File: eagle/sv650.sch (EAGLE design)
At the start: 22 parts, among them IC1 7805

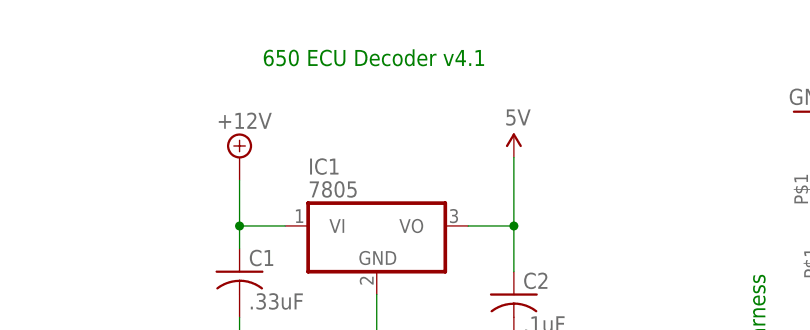
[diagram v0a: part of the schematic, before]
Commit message: update to show v4.2 and date
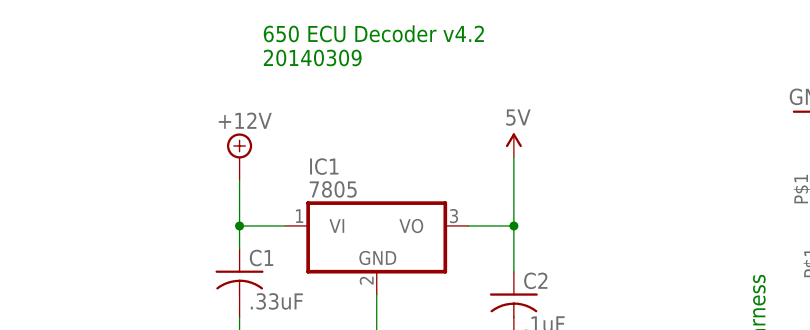
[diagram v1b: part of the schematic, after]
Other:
- note added: "650 ECU Decoder v4.2 20140309"
- note removed: "650 ECU Decoder v4.1"
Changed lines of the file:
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@@
 <plain>
 <text x="114.3" y="68.58" size="1.778" layer="91" rot="R90">To Wiring Harness</text>
-<text x="58.42" y="111.76" size="1.778" layer="91">650 ECU Decoder v4.1</text>
+<text x="58.42" y="111.76" size="1.778" layer="91">650 ECU Decoder v4.2
+20140309</text>
 </plain>
 <instances>
@@
 </schematic>
 </drawing>
+<compatibility>
+<note version="6.3" minversion="6.2.2" severity="warning">
+Since Version 6.2.2 text objects can contain more than one line,
+which will not be processed correctly with this version.
+</note>
+</compatibility>
 </eagle>

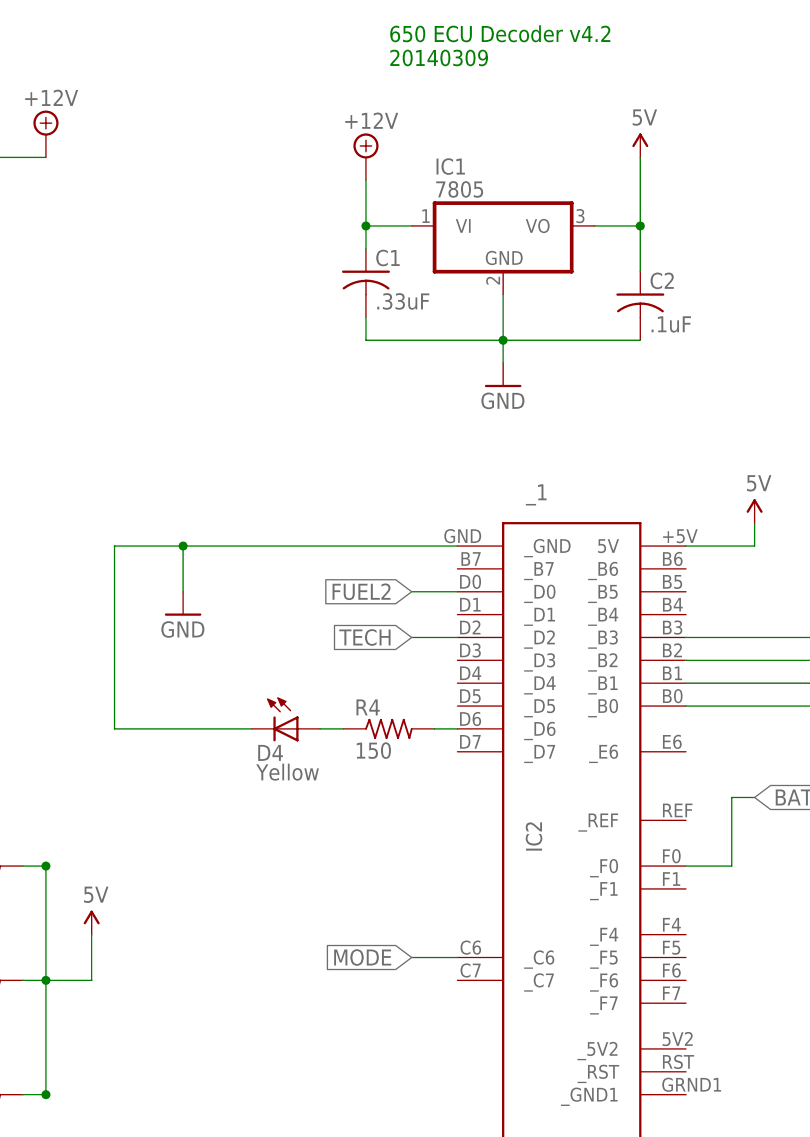
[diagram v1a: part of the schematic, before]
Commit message: change mode button to pin D1/6 so we can assign an interrupt to it
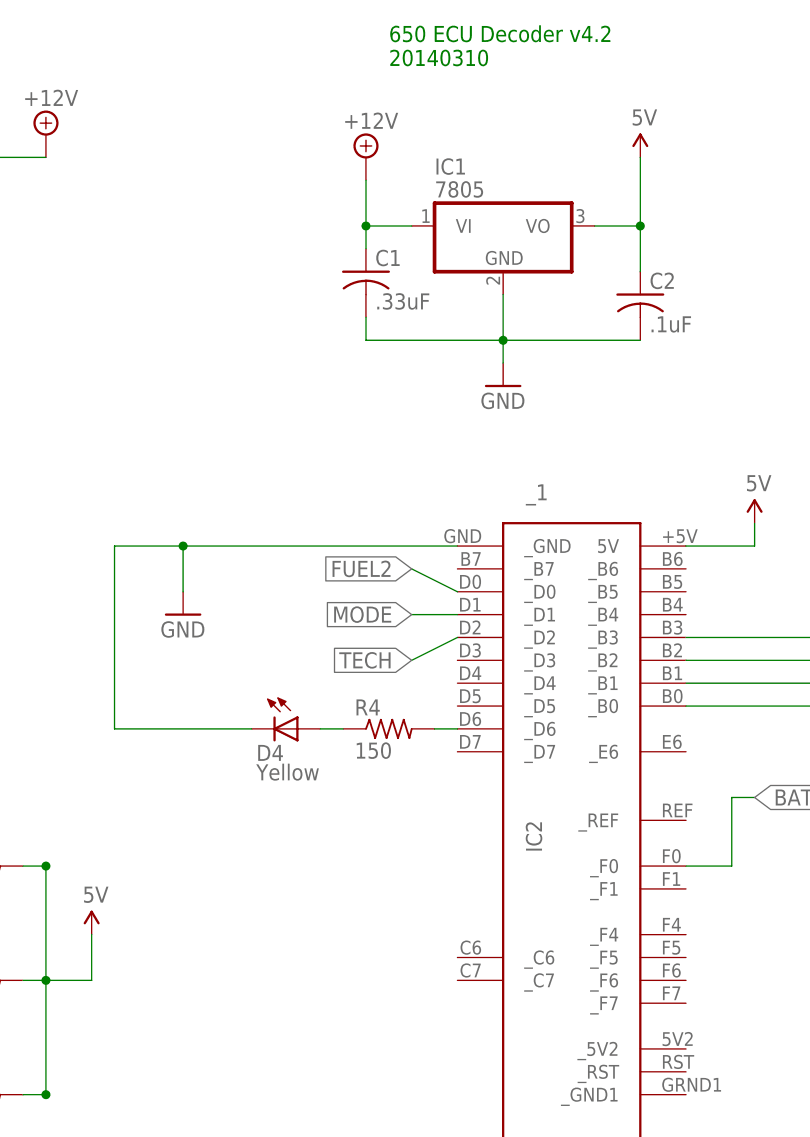
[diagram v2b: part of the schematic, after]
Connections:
- net MODE: now also _1._D1; no longer _1._C6
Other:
- note added: "650 ECU Decoder v4.2 20140310"
- note removed: "650 ECU Decoder v4.2 20140309"
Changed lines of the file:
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@@
 <text x="114.3" y="68.58" size="1.778" layer="91" rot="R90">To Wiring Harness</text>
 <text x="58.42" y="111.76" size="1.778" layer="91">650 ECU Decoder v4.2
-20140309</text>
+20140310</text>
 </plain>
 <instances>
@@
 <segment>
 <pinref part="_1" gate="G$1" pin="_D2"/>
-<wire x1="66.04" y1="48.26" x2="60.96" y2="48.26" width="0.1524" layer="91"/>
-<label x="60.96" y="48.26" size="1.778" layer="95" rot="R180" xref="yes"/>
+<wire x1="66.04" y1="48.26" x2="60.96" y2="45.72" width="0.1524" layer="91"/>
+<label x="60.96" y="45.72" size="1.778" layer="95" rot="R180" xref="yes"/>
 </segment>
 </net>
@@
 </segment>
 <segment>
-<pinref part="_1" gate="G$1" pin="_C6"/>
-<wire x1="66.04" y1="12.7" x2="60.96" y2="12.7" width="0.1524" layer="91"/>
-<label x="60.96" y="12.7" size="1.778" layer="95" rot="R180" xref="yes"/>
+<pinref part="_1" gate="G$1" pin="_D1"/>
+<wire x1="66.04" y1="50.8" x2="60.96" y2="50.8" width="0.1524" layer="91"/>
+<label x="60.96" y="50.8" size="1.778" layer="95" rot="R180" xref="yes"/>
 </segment>
 </net>
@@
 <segment>
 <pinref part="_1" gate="G$1" pin="_D0"/>
-<wire x1="66.04" y1="53.34" x2="60.96" y2="53.34" width="0.1524" layer="91"/>
-<label x="60.96" y="53.34" size="1.778" layer="95" rot="R180" xref="yes"/>
-</segment>
-</net>
+<wire x1="66.04" y1="53.34" x2="60.96" y2="55.88" width="0.1524" layer="91"/>
+<label x="60.96" y="55.88" size="1.778" layer="95" rot="R180" xref="yes"/>
+</segment>
+</net>

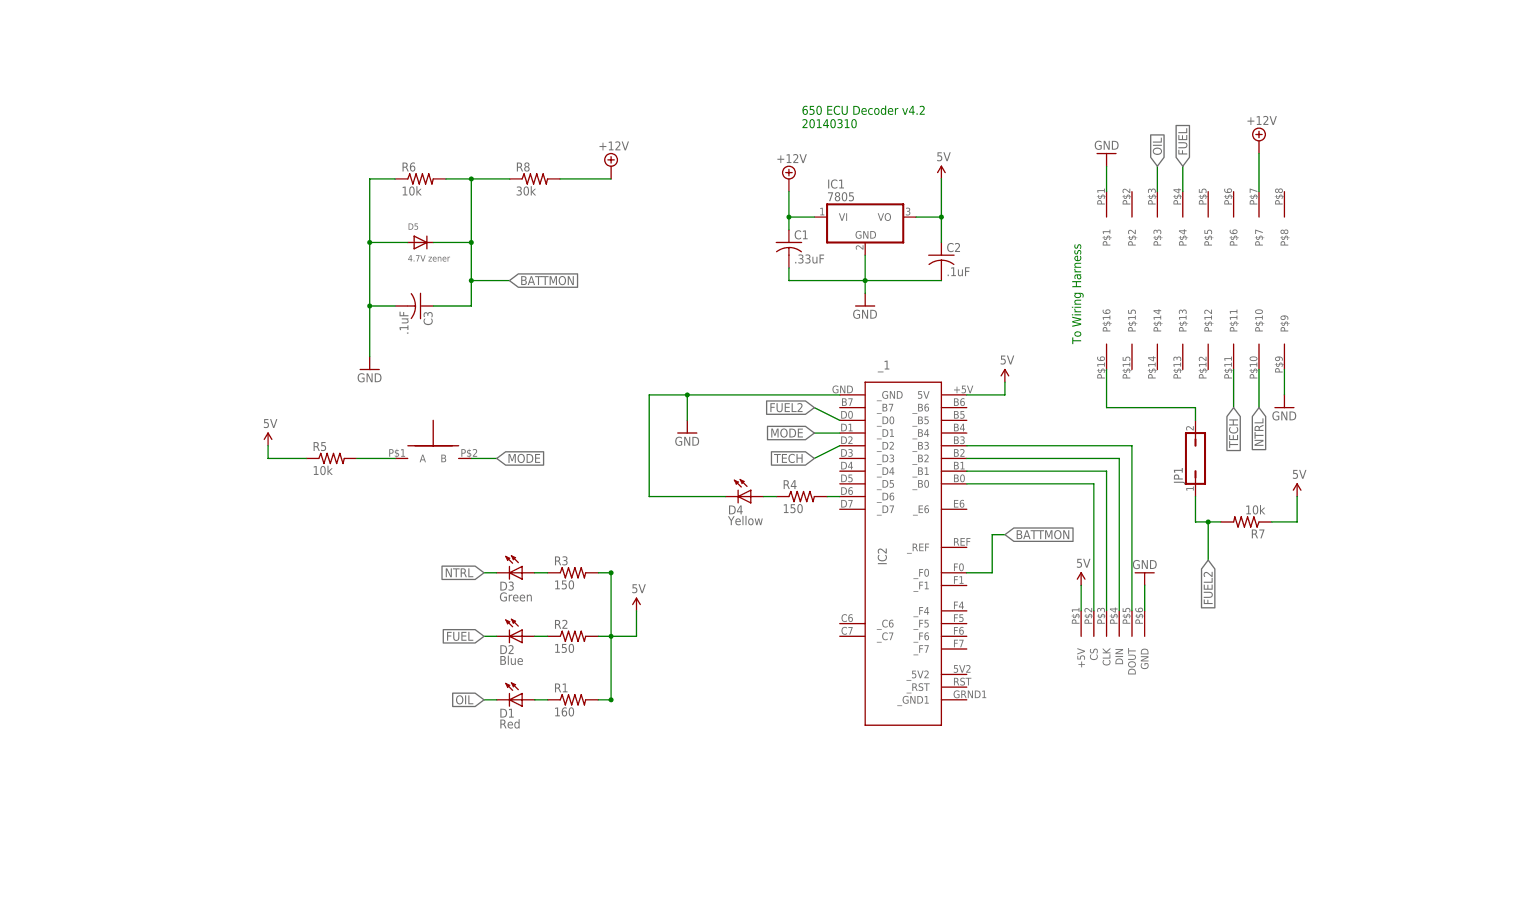
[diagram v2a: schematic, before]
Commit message: - update board to v4.2 with LM7805 w/ heat sink - fix mode button to use a pin supporting interrupts - remove external pullup resistors
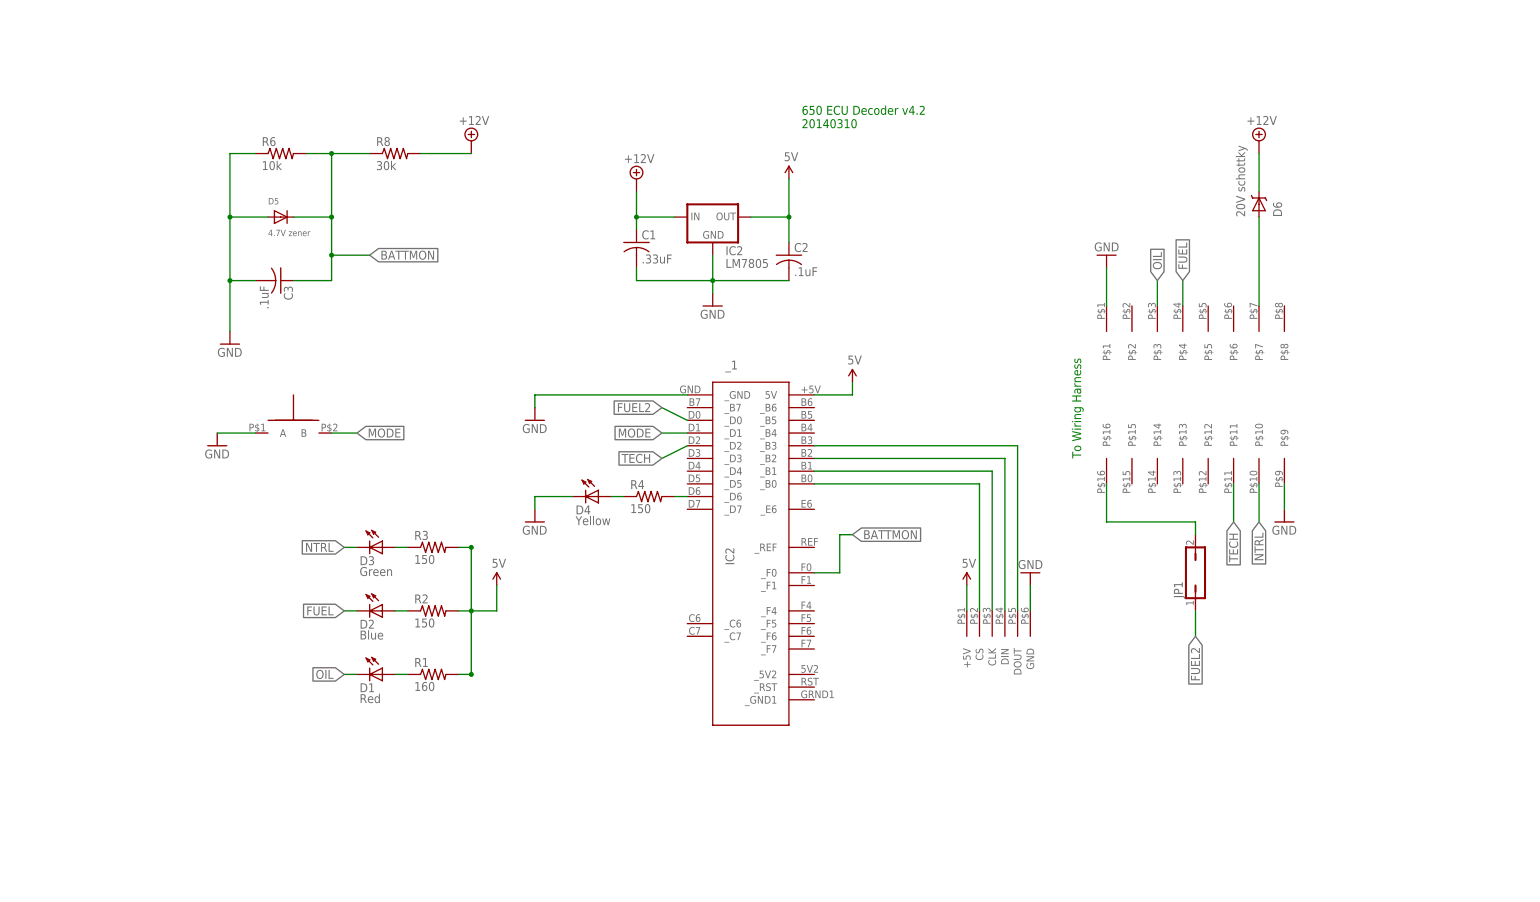
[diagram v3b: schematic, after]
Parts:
- removed IC1: 7805, linear:78TH2
- removed R5, R7: 10k, resistor:R-US_M0805
- added D6: 20V schottky, synfinatic:SCHOTTKY-DIODESOD-123
- added IC2: LM7805, synfinatic:V_REG_78XXFLATSINK
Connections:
- net +12V: now also D6.C, IC2.IN; no longer IC1.VI, U$3.P$7
- net 5V: now also IC2.OUT; no longer IC1.VO, R5.1, R7.1
- net FUEL2: no longer R7.2
- net GND: now also IC2.GND, U$10.A; no longer IC1.GND
- net N$12: now also D6.A, U$3.P$7; no longer R5.2, U$10.A
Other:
- moved on the sheet: C1, C2, C3, D1, D2, D3, D4, D5, JP1, R1, R2, R3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

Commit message: update board to v4.3 - switch to LM2674-5.0 - Fix 20V schottky diode
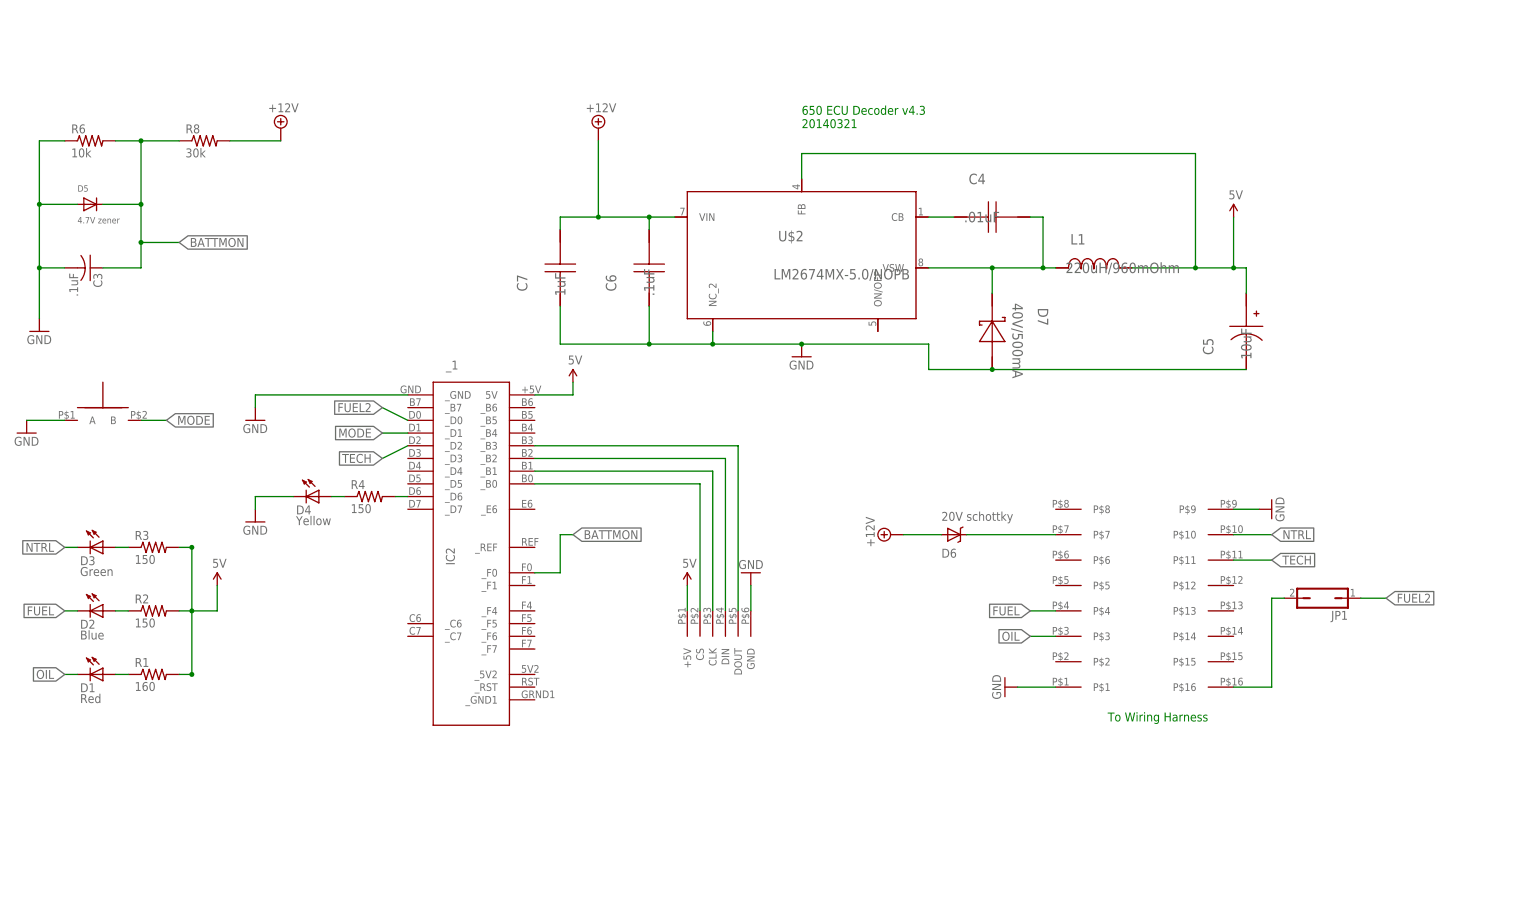
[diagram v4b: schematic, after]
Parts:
- removed C1: .33uF, adafruit:C-US025-024X044
- removed C2: .1uF, adafruit:C-US025-024X044
- removed IC2: LM7805, synfinatic:V_REG_78XXFLATSINK
- added C4: .01uF, TI-LM2674:GRM216R71H103KA01D
- added C5: 10uF, TI-LM2674:EEE-FK1V100R
- added C6: .1uF, TI-LM2674:08053C104KAT2A
- added C7: 1uF, TI-LM2674:C3216X7R1H105K
- added D7: 40V/500mA, TI-LM2674:MBR0540T1G
- added L1: 220uH/960mOhm, TI-LM2674:SDR0805-221KL
- added U$2: LM2674MX-5.0/NOPB, TI-LM2674:LM2674MX-5.0/NOPB
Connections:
- new net N$13: C4.2, U$2.CB
- new net N$14: C4.1, D7.K, L1.2, U$2.VSW
- net +12V: now also C6.1, C7.1, D6.A, U$2.VIN; no longer C1.1, D6.C, IC2.IN
- net 5V: now also C5.+, L1.1, U$2.FB; no longer C2.1, IC2.OUT
- net GND: now also C5.-, C6.2, C7.2, D7.A, U$2.NC_2; no longer C1.2, C2.2, IC2.GND
- net N$12: now also D6.C; no longer D6.A
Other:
- note added: "650 ECU Decoder v4.3 20140321"
- note removed: "650 ECU Decoder v4.2 20140310"
- moved on the sheet: C3, D1, D2, D3, D4, D5, D6, JP1, R1, R2, R3, R4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
